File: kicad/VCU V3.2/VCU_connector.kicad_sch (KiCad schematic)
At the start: 2 parts

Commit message: pudh
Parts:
- renumbered J2 to J?, J1 to J?
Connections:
- net +12V: now also J?.1, J?.1, J?.2, J?.2; no longer J?.10, J?.17, J?.18, J?.9
- net +5V: now also J?.3; no longer J?.19
- net APPS_3VGND: now also J?.2; no longer J?.18
- net APPS_3VOUT: now also J?.2; no longer J?.10
- net APPS_5VGND: now also J?.1; no longer J?.17
- net APPS_5VOUT: now also J?.1; no longer J?.9
- net BRAKE_AIN: now also J?.3; no longer J?.11
- net CANH_2: now also J?.8; no longer J?.16
- net CANH_3: now also J?.6; no longer J?.14
- net CANL_2: now also J?.7; no longer J?.15
- net CANL_3: now also J?.5; no longer J?.13
- net CURRENT_AIN: now also J?.4; no longer J?.12
- net DIN_1: now also J?.5; no longer J?.21
- net DIN_2: now also J?.6; no longer J?.22
- net DIN_3: now also J?.7; no longer J?.23
- net GND: now also J?.3, J?.4, J?.7, J?.7, J?.8, J?.8; no longer J?.15, J?.16, J?.19, J?.20, J?.23, J?.24
- net IGN_12V: now also J?.8; no longer J?.24
- net PDU_1: now also J?.3; no longer J?.11
- net PDU_2: now also J?.4; no longer J?.12
- net PDU_3: now also J?.5; no longer J?.13
- net PDU_4: now also J?.6; no longer J?.14
- net PDU_5: now also J?.4; no longer J?.20
- net PDU_6: now also J?.5; no longer J?.21
- net PDU_7: now also J?.6; no longer J?.22
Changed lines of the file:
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@@
 		(dnp no)
 		(fields_autoplaced yes)
-		(property "Reference" "#PWR04"
+		(property "Reference" "#PWR?"
 			(at 90.17 76.2 0)
 			(effects
@@
 		(dnp no)
 		(fields_autoplaced yes)
-		(property "Reference" "#PWR015"
+		(property "Reference" "#PWR?"
 			(at 143.51 76.2 0)
 			(effects
@@
 		(dnp no)
 		(fields_autoplaced yes)
-		(property "Reference" "#PWR08"
+		(property "Reference" "#PWR?"
 			(at 99.06 81.28 0)
 			(effects
@@
 		(dnp no)
 		(fields_autoplaced yes)
-		(property "Reference" "#PWR010"
+		(property "Reference" "#PWR?"
 			(at 102.87 116.84 0)
 			(effects
@@
 		(lib_id "HD241:HD241")
 		(at 105.41 102.87 0)
-		(unit 2)
-		(exclude_from_sim no)
-		(in_bom yes)
-		(on_board yes)
-		(dnp no)
-		(fields_autoplaced yes)
-		(property "Reference" "J2"
+		(unit 1)
+		(exclude_from_sim no)
+		(in_bom yes)
+		(on_board yes)
+		(dnp no)
+		(fields_autoplaced yes)
+		(property "Reference" "J?"
 			(at 109.855 100.203 0)
 			(effects
@@
 		(dnp no)
 		(fields_autoplaced yes)
-		(property "Reference" "J2"
+		(property "Reference" "J?"
 			(at 136.525 100.33 0)
 			(effects
@@
 		(dnp no)
 		(fields_autoplaced yes)
-		(property "Reference" "#PWR05"
+		(property "Reference" "#PWR?"
 			(at 90.17 96.52 0)
 			(effects
@@
 		(lib_id "HD241:HD241")
 		(at 78.74 69.85 0)
-		(unit 3)
-		(exclude_from_sim no)
-		(in_bom yes)
-		(on_board yes)
-		(dnp no)
-		(fields_autoplaced yes)
-		(property "Reference" "J1"
+		(unit 1)
+		(exclude_from_sim no)
+		(in_bom yes)
+		(on_board yes)
+		(dnp no)
+		(fields_autoplaced yes)
+		(property "Reference" "J?"
 			(at 83.185 67.691 0)
 			(effects
@@
 		(dnp no)
 		(fields_autoplaced yes)
-		(property "Reference" "#PWR018"
+		(property "Reference" "#PWR?"
 			(at 160.02 116.84 0)
 			(effects
@@
 		(lib_id "HD241:HD241")
 		(at 105.41 69.85 0)
-		(unit 2)
-		(exclude_from_sim no)
-		(in_bom yes)
-		(on_board yes)
-		(dnp no)
-		(fields_autoplaced yes)
-		(property "Reference" "J1"
+		(unit 1)
+		(exclude_from_sim no)
+		(in_bom yes)
+		(on_board yes)
+		(dnp no)
+		(fields_autoplaced yes)
+		(property "Reference" "J?"
 			(at 109.855 67.183 0)
 			(effects
@@
 		(dnp no)
 		(fields_autoplaced yes)
-		(property "Reference" "J1"
+		(property "Reference" "J?"
 			(at 136.525 67.31 0)
 			(effects
@@
 		(dnp no)
 		(fields_autoplaced yes)
-		(property "Reference" "#PWR016"
+		(property "Reference" "#PWR?"
 			(at 143.51 96.52 0)
 			(effects
@@
 		(dnp no)
 		(fields_autoplaced yes)
-		(property "Reference" "#PWR013"
+		(property "Reference" "#PWR?"
 			(at 116.84 76.2 0)
 			(effects
@@
 		(lib_id "HD241:HD241")
 		(at 78.74 102.87 0)
-		(unit 3)
-		(exclude_from_sim no)
-		(in_bom yes)
-		(on_board yes)
-		(dnp no)
-		(fields_autoplaced yes)
-		(property "Reference" "J2"
+		(unit 1)
+		(exclude_from_sim no)
+		(in_bom yes)
+		(on_board yes)
+		(dnp no)
+		(fields_autoplaced yes)
+		(property "Reference" "J?"
 			(at 83.185 100.711 0)
 			(effects
@@
 		(dnp no)
 		(fields_autoplaced yes)
-		(property "Reference" "#PWR014"
+		(property "Reference" "#PWR?"
 			(at 116.84 96.52 0)
 			(effects

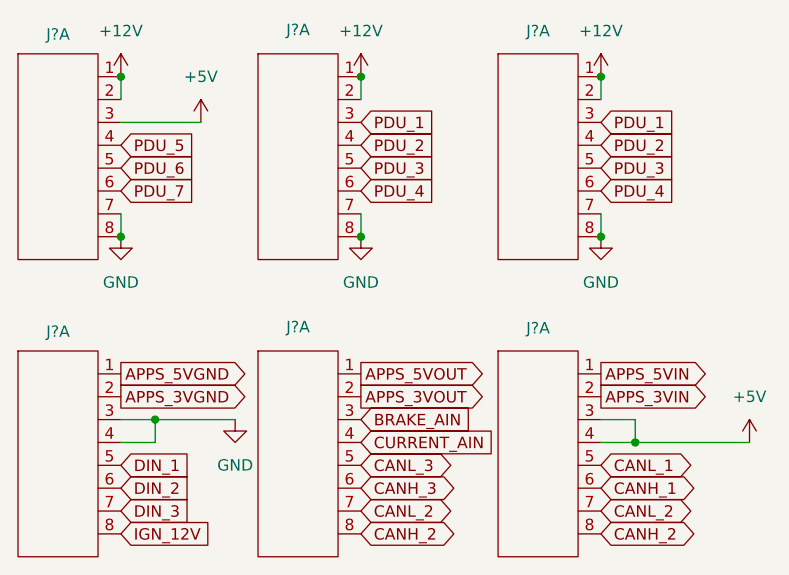
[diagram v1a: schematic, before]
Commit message: what
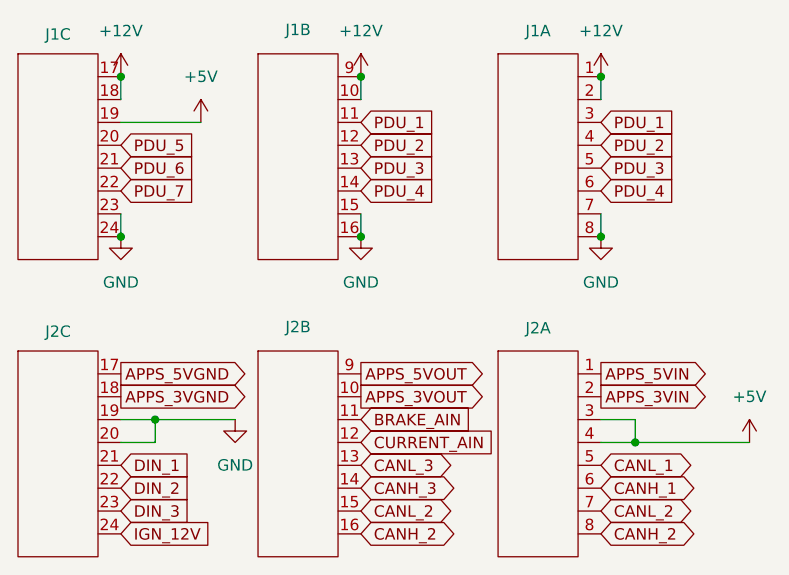
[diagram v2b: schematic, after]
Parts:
- gave numbers to parts that had none: 2
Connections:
- net +12V: now also J1.10, J1.17, J1.18, J1.9; no longer J1.1, J1.1, J1.2, J1.2
- net +5V: now also J1.19; no longer J1.3
- net APPS_3VGND: now also J2.18; no longer J2.2
- net APPS_3VOUT: now also J2.10; no longer J2.2
- net APPS_5VGND: now also J2.17; no longer J2.1
- net APPS_5VOUT: now also J2.9; no longer J2.1
- net BRAKE_AIN: now also J2.11; no longer J2.3
- net CANH_2: now also J2.16; no longer J2.8
- net CANH_3: now also J2.14; no longer J2.6
- net CANL_2: now also J2.15; no longer J2.7
- net CANL_3: now also J2.13; no longer J2.5
- net CURRENT_AIN: now also J2.12; no longer J2.4
- net DIN_1: now also J2.21; no longer J2.5
- net DIN_2: now also J2.22; no longer J2.6
- net DIN_3: now also J2.23; no longer J2.7
- net GND: now also J1.15, J1.16, J1.23, J1.24, J2.19, J2.20; no longer J1.7, J1.7, J1.8, J1.8, J2.3, J2.4
- net IGN_12V: now also J2.24; no longer J2.8
- net PDU_1: now also J1.11; no longer J1.3
- net PDU_2: now also J1.12; no longer J1.4
- net PDU_3: now also J1.13; no longer J1.5
- net PDU_4: now also J1.14; no longer J1.6
- net PDU_5: now also J1.20; no longer J1.4
- net PDU_6: now also J1.21; no longer J1.5
- net PDU_7: now also J1.22; no longer J1.6
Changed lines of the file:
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@@
 		(dnp no)
 		(fields_autoplaced yes)
-		(property "Reference" "#PWR?"
+		(property "Reference" "#PWR04"
 			(at 90.17 76.2 0)
 			(effects
@@
 		(dnp no)
 		(fields_autoplaced yes)
-		(property "Reference" "#PWR?"
+		(property "Reference" "#PWR015"
 			(at 143.51 76.2 0)
 			(effects
@@
 		(dnp no)
 		(fields_autoplaced yes)
-		(property "Reference" "#PWR?"
+		(property "Reference" "#PWR08"
 			(at 99.06 81.28 0)
 			(effects
@@
 		(dnp no)
 		(fields_autoplaced yes)
-		(property "Reference" "#PWR?"
+		(property "Reference" "#PWR010"
 			(at 102.87 116.84 0)
 			(effects
@@
 		(lib_id "HD241:HD241")
 		(at 105.41 102.87 0)
-		(unit 1)
-		(exclude_from_sim no)
-		(in_bom yes)
-		(on_board yes)
-		(dnp no)
-		(fields_autoplaced yes)
-		(property "Reference" "J?"
+		(unit 2)
+		(exclude_from_sim no)
+		(in_bom yes)
+		(on_board yes)
+		(dnp no)
+		(fields_autoplaced yes)
+		(property "Reference" "J2"
 			(at 109.855 100.203 0)
 			(effects
@@
 		(dnp no)
 		(fields_autoplaced yes)
-		(property "Reference" "J?"
+		(property "Reference" "J2"
 			(at 136.525 100.33 0)
 			(effects
@@
 		(dnp no)
 		(fields_autoplaced yes)
-		(property "Reference" "#PWR?"
+		(property "Reference" "#PWR05"
 			(at 90.17 96.52 0)
 			(effects
@@
 		(lib_id "HD241:HD241")
 		(at 78.74 69.85 0)
-		(unit 1)
-		(exclude_from_sim no)
-		(in_bom yes)
-		(on_board yes)
-		(dnp no)
-		(fields_autoplaced yes)
-		(property "Reference" "J?"
+		(unit 3)
+		(exclude_from_sim no)
+		(in_bom yes)
+		(on_board yes)
+		(dnp no)
+		(fields_autoplaced yes)
+		(property "Reference" "J1"
 			(at 83.185 67.691 0)
 			(effects
@@
 		(dnp no)
 		(fields_autoplaced yes)
-		(property "Reference" "#PWR?"
+		(property "Reference" "#PWR018"
 			(at 160.02 116.84 0)
 			(effects
@@
 		(lib_id "HD241:HD241")
 		(at 105.41 69.85 0)
-		(unit 1)
-		(exclude_from_sim no)
-		(in_bom yes)
-		(on_board yes)
-		(dnp no)
-		(fields_autoplaced yes)
-		(property "Reference" "J?"
+		(unit 2)
+		(exclude_from_sim no)
+		(in_bom yes)
+		(on_board yes)
+		(dnp no)
+		(fields_autoplaced yes)
+		(property "Reference" "J1"
 			(at 109.855 67.183 0)
 			(effects
@@
 		(dnp no)
 		(fields_autoplaced yes)
-		(property "Reference" "J?"
+		(property "Reference" "J1"
 			(at 136.525 67.31 0)
 			(effects
@@
 		(dnp no)
 		(fields_autoplaced yes)
-		(property "Reference" "#PWR?"
+		(property "Reference" "#PWR016"
 			(at 143.51 96.52 0)
 			(effects
@@
 		(dnp no)
 		(fields_autoplaced yes)
-		(property "Reference" "#PWR?"
+		(property "Reference" "#PWR013"
 			(at 116.84 76.2 0)
 			(effects
@@
 		(lib_id "HD241:HD241")
 		(at 78.74 102.87 0)
-		(unit 1)
-		(exclude_from_sim no)
-		(in_bom yes)
-		(on_board yes)
-		(dnp no)
-		(fields_autoplaced yes)
-		(property "Reference" "J?"
+		(unit 3)
+		(exclude_from_sim no)
+		(in_bom yes)
+		(on_board yes)
+		(dnp no)
+		(fields_autoplaced yes)
+		(property "Reference" "J2"
 			(at 83.185 100.711 0)
 			(effects
@@
 		(dnp no)
 		(fields_autoplaced yes)
-		(property "Reference" "#PWR?"
+		(property "Reference" "#PWR014"
 			(at 116.84 96.52 0)
 			(effects
